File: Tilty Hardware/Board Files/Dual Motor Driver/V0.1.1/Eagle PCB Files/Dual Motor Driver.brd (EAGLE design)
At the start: 50.8 x 50.8 mm, 33 parts, among them J1 AVR_SPI_PRG_6PTH, Q1 16MHz, U1 ATMEGA328P, U2 L298_BRIDGE_DRIVER, U5 VOLTAGE-REGULATOR

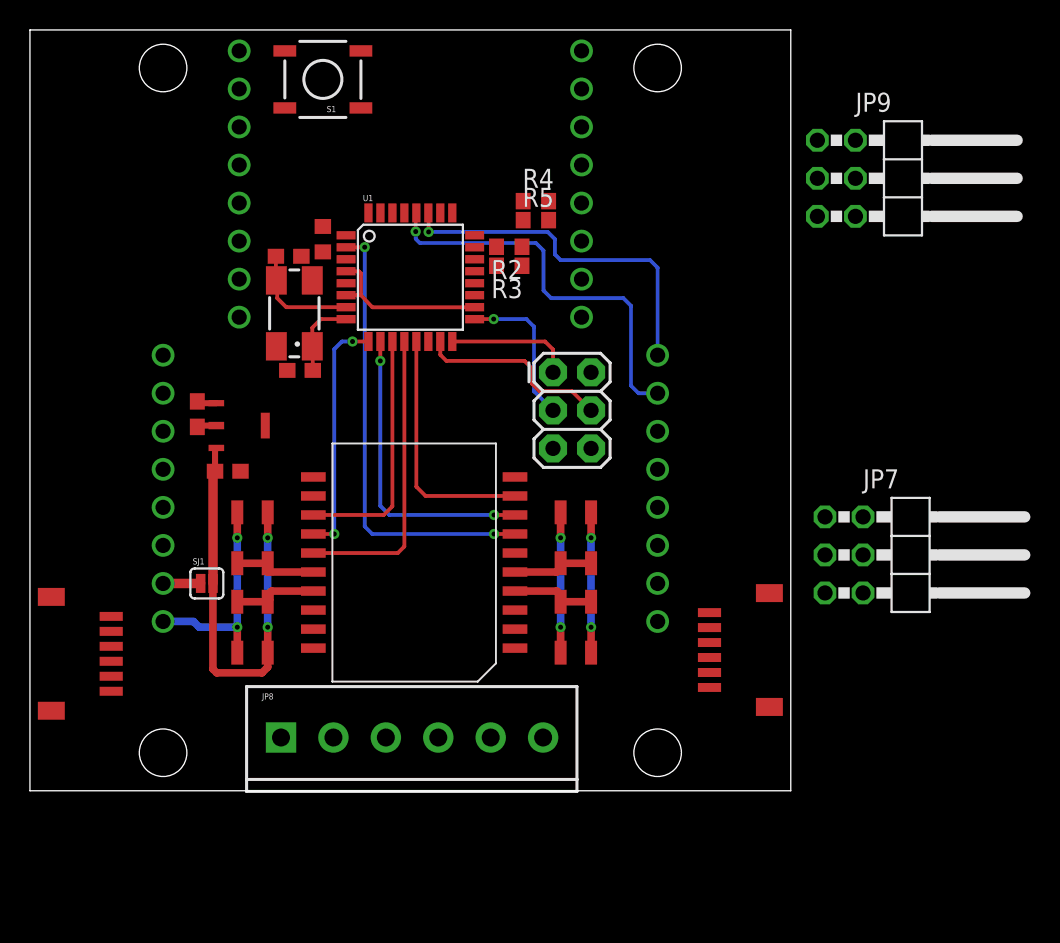
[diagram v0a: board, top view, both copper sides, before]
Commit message: Finished Tilty Duo/Quad 0.2.4, work on motor driver
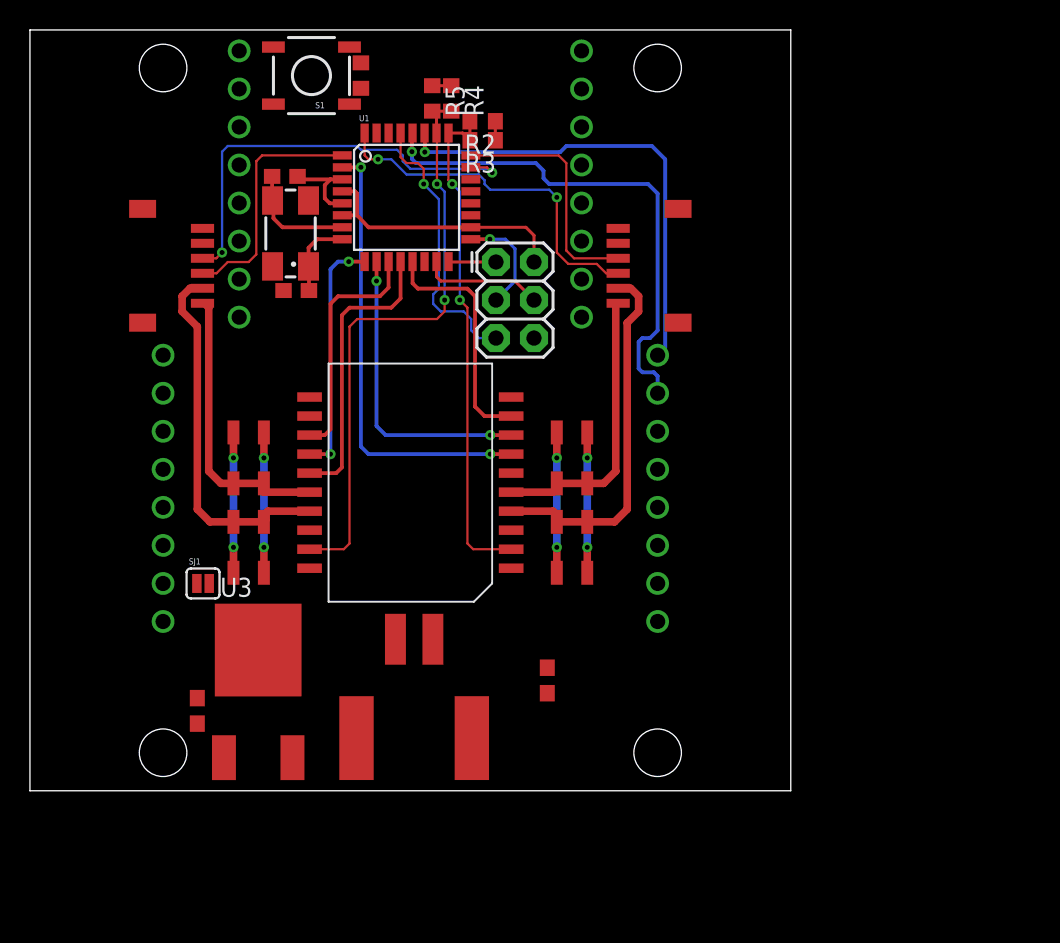
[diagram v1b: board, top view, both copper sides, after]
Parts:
- removed JP8: (no value), SparkFun-Connectors:SCREWTERMINAL-3.5MM-6
- removed JP9: (no value), pinhead:2X03/90
- removed U5: VOLTAGE-REGULATOR, My Parts:SOT89
- added U3: LM2931, on-semiconductor:TO263
- C6: value 0.1uF -> 4.7uF
- C7: value 1uF -> 0.1uF
- JP7: value (none) -> 2-POS_SMD_TERM_BLOCK; device pinhead:2X03/90 -> My Parts:2-POS_SMD_TERMINAL_BLOCK
- moved JP7 35.2 mm to (25.7, 5.84), turned to 0 degrees
- moved C6 29.4 mm to (34.5, 7.37), turned to 90 degrees
- moved JP5 26.6 mm to (9.40, 35.1)
- moved JP6 26.4 mm to (41.4, 35.1)
- moved C7 16.1 mm to (11.2, 5.33), turned to 90 degrees
- moved R1 11.2 mm to (22.1, 47.8)
- moved R5 10.7 mm to (26.9, 46.2), turned to 270 degrees
- moved R4 8.89 mm to (28.1, 46.2), turned to 270 degrees
- moved R2 8.57 mm to (30.2, 44.7)
- moved R3 8.57 mm to (30.2, 43.4)
- moved J1 8.29 mm to (31.1, 35.3)
- moved D2 5.34 mm to (37.2, 22.2)
- moved C2 5.34 mm to (17.8, 33.4)
- moved C8 5.34 mm to (17.0, 41.0)
- moved D3 5.34 mm to (13.6, 22.2)
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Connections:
- net +24V: now also JP7.P$3, U3.P$2; no longer JP8.4, U5.P$3
- net +5V: now also U3.P$3; no longer U5.P$1
- net ENC1B: now also U1.24
- net ENC2A: now also JP5.P$3, U1.23; no longer JP5.P$4, U1.1
- net ENC2B: now also JP5.P$4, U1.1; no longer JP5.P$3
- net GND: now also JP7.P$4, U3.P$1; no longer JP8.3, U5.P$2, U5.P$4
- net M1A: now also JP6.P$2; no longer JP6.P$1, JP8.6
- net M1B: now also JP6.P$1; no longer JP6.P$2, JP8.5
- net M2A: now also JP5.P$6; no longer JP5.P$5, JP8.2
- net M2B: now also JP5.P$5; no longer JP5.P$6, JP8.1
- net SENSE_1: now also U1.25; no longer U1.23
- net SENSE_2: now also U1.26; no longer U1.24
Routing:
- net SENSE_2: track 0.00 -> 39.1 mm, vias 0 -> 2
- net SENSE_1: track 0.00 -> 33.9 mm, vias 0 -> 2
- net ENC2A: track 0.00 -> 28.9 mm, vias 0 -> 2
- net ENC1A: track 0.00 -> 24.0 mm, vias 0 -> 2
- net +24V: track 38.5 -> 18.7 mm
- net M1A: track 5.64 -> 24.8 mm
- net M2B: track 5.64 -> 24.6 mm
- net RESET: track 0.00 -> 18.7 mm, vias 0 -> 1
- net ENC2B: track 0.00 -> 16.2 mm
- net ENC1B: track 0.00 -> 16.1 mm
- net M1B: track 5.52 -> 19.1 mm
- net M2A: track 5.77 -> 19.2 mm
- net SCL: track 26.9 -> 34.5 mm
- net SDA: track 24.0 -> 31.2 mm
- net MISO: track 8.47 -> 3.18 mm
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
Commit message: Nearly finalized dual motor driver add-on
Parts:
- added D10: (no value), SparkFun-LED:LED-0805
- added D9: (no value), diode:DO214AA
- added JP10, JP9: (no value), SparkFun-Connectors:1X02
- added JP8: (no value), SparkFun-Connectors:1X04_LOCK
- added R6: (no value), resistor:R0603
- added SJ2: (no value), SparkFun-Passives:SJ_2S-TRACE
- JP1, JP2, JP3, JP4: value (none) -> 8-PIN_HEADER; device pinhead:1X08_NO_SS -> My Parts:8-PIN_RECEPTACLE_LOCK_NO-SS
- moved C7 18.4 mm to (28.4, 11.7), turned to 270 degrees
- moved U3 12.6 mm to (27.8, 6.35), turned to 180 degrees
- moved C6 8.54 mm to (27.2, 11.7), turned to 270 degrees
- moved JP7 6.48 mm to (19.2, 5.59)
- moved D7 6.22 mm to (29.0, 22.2)
- moved D8 6.22 mm to (29.0, 16.3)
- moved R4 6.22 mm to (21.9, 46.2)
- moved U1 6.22 mm to (18.9, 39.6)
- moved C2 6.22 mm to (11.6, 33.4)
- moved C8 6.22 mm to (10.8, 41.0)
- moved D3 6.22 mm to (7.37, 22.2)
- moved D4 6.22 mm to (7.37, 16.3)
- moved D5 6.22 mm to (9.40, 16.3)
- moved D6 6.22 mm to (9.40, 22.2)
- moved JP1 6.22 mm to (7.75, 40.5)
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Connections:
- new net N$1: D10.1, R6.2
- new net N$3: C7.1, D9.A, SJ2.1, U3.P$2
- new net RX: JP8.3, U1.30
- new net TX: JP8.4, U1.31
- net +24V: now also D9.C, SJ2.2; no longer C7.1, U3.P$2
- net +5V: now also JP4.P$1, JP8.1, R6.1; no longer JP4.1
- net GND: now also D10.2, JP2.P$1, JP3.P$1, JP4.P$2, JP8.2, U2.20; no longer JP2.1, JP3.1, JP4.2
- net M1A: now also JP9.2
- net M1B: now also JP9.1
- net M2A: now also JP10.2
- net M2B: now also JP10.1
- net N$5: now also JP2.P$2; no longer JP2.2
- net SCL: now also JP3.P$7; no longer JP3.7
- net SDA: now also JP3.P$8; no longer JP3.8
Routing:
- net GND: track 27.1 -> 276.5 mm, vias 4 -> 20
- net +5V: track 17.7 -> 148.8 mm, vias 0 -> 6
- net +24V: track 18.7 -> 63.7 mm
- net M1B: track 19.1 -> 40.2 mm, vias 0 -> 1
- net M2A: track 19.2 -> 34.4 mm, vias 0 -> 1
- net M1A: track 24.8 -> 37.1 mm
- net M2B: track 24.6 -> 34.4 mm
- net RESET: track 18.7 -> 28.3 mm
- net N$5: track 0.00 -> 8.34 mm
- net N$3: track 0.00 -> 7.67 mm
- net RX: track 0.00 -> 7.36 mm, vias 0 -> 1
- net TX: track 0.00 -> 6.03 mm, vias 0 -> 1
- net N$1: track 0.00 -> 1.86 mm
- net SDA: track 31.2 -> 29.4 mm
- net SCL: track 34.5 -> 32.9 mm
- added copper zone on layer 1, net GND
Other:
- board size 50.8 x 50.8 mm -> 38.4 x 50.8 mm
- board text added: "+"
- board text added: "-"
- board text added: "5v"
- board text added: "Driver Add-on"
- board text added: "Dual Motor"
- board text added: "GND"
- board text added: "ICSP"
- board text added: "IMU"
- board text added: "M1A"
- board text added: "M1B"
- board text added: "M2A"
- board text added: "M2B"
- board text added: "PWR"
- board text added: "Reset"
- board text added: "Rx"
- board text added: "SJ1"
- board text added: "Tx"

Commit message: New RC Receiver add-on testing code and minor motor driver updates
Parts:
- J1: value AVR_SPI_PRG_6PTH -> AVR_SPI_PRG_62X3_LOCK; device SparkFun-Connectors:2X3 -> SparkFun-Connectors:2X3_LOCK
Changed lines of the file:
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@@
 <attribute name="PART#" value="SM06B-SRSS-TB(LF)(SN)" x="35.179" y="35.052" size="1.778" layer="27" rot="R90" display="off"/>
 </element>
-<element name="J1" library="SparkFun-Connectors" package="2X3" value="AVR_SPI_PRG_6PTH" x="24.892" y="35.306" smashed="yes" rot="R270"/>
+<element name="J1" library="SparkFun-Connectors" package="2X3_LOCK" value="AVR_SPI_PRG_62X3_LOCK" x="24.892" y="35.306" smashed="yes" rot="R270"/>
 <element name="R1" library="resistor" package="R0603" value="10K" x="19.3675" y="46.228" smashed="yes" rot="R90"/>
 <element name="C6" library="resistor" package="C0603" value="4.7uF" x="27.178" y="11.684" smashed="yes" rot="R270"/>
@@
 <wire x1="24.4856" y1="36.83" x2="23.2216" y2="36.83" width="0.254" layer="1"/>
 <wire x1="23.2216" y1="36.83" x2="23.2156" y2="36.824" width="0.254" layer="1"/>
-<wire x1="24.892" y1="32.766" x2="26.162" y2="34.036" width="0.2032" layer="16"/>
+<wire x1="24.638" y1="32.766" x2="26.162" y2="34.036" width="0.2032" layer="16"/>
 <wire x1="26.162" y1="34.036" x2="26.162" y2="36.195" width="0.2032" layer="16"/>
 <wire x1="26.162" y1="36.195" x2="25.527" y2="36.83" width="0.2032" layer="16"/>
@@
 <wire x1="20.923" y1="34.322" x2="21.209" y2="34.036" width="0.2032" layer="1"/>
 <wire x1="21.209" y1="34.036" x2="26.162" y2="34.036" width="0.2032" layer="1"/>
-<wire x1="26.162" y1="34.036" x2="27.432" y2="32.766" width="0.2032" layer="1"/>
+<wire x1="26.162" y1="34.036" x2="27.178" y2="32.766" width="0.2032" layer="1"/>
 </signal>
 <signal name="MISO">
@@
 <contactref element="U1" pad="13"/>
 <wire x1="25.908" y1="25.019" x2="24.13" y2="25.019" width="0.254" layer="1"/>
-<wire x1="24.13" y1="25.019" x2="23.495" y2="25.654" width="0.254" layer="1"/>
-<wire x1="23.495" y1="25.654" x2="23.495" y2="33.02" width="0.254" layer="1"/>
-<wire x1="23.495" y1="33.02" x2="22.987" y2="33.528" width="0.254" layer="1"/>
+<wire x1="24.13" y1="25.019" x2="23.4315" y2="25.7175" width="0.254" layer="1"/>
+<wire x1="23.4315" y1="25.7175" x2="23.368" y2="33.147" width="0.254" layer="1"/>
+<wire x1="23.368" y1="33.147" x2="22.987" y2="33.528" width="0.254" layer="1"/>
 <wire x1="19.323" y1="35.3314" x2="19.323" y2="33.89" width="0.254" layer="1"/>
 <wire x1="19.323" y1="33.89" x2="19.685" y2="33.528" width="0.254" layer="1"/>

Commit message: Tilty Omni work!
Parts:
- moved D10 0.97 mm to (11.2, 2.92), turned to 180 degrees
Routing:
- net GND: track 276.5 -> 274.4 mm
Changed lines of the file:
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@@
 <text x="18.415" y="48.1965" size="1.524" layer="26" ratio="10" rot="MR270">Tx</text>
 <text x="17.907" y="29.464" size="1.651" layer="25" ratio="12">ICSP</text>
-<text x="6.477" y="1.778" size="1.651" layer="25" ratio="12">PWR</text>
+<text x="6.985" y="4.318" size="1.651" layer="25" ratio="12">PWR</text>
 <rectangle x1="23.13594375" y1="18.232378125" x2="23.27818125" y2="18.252696875" layer="26" rot="R213"/>
 <rectangle x1="23.10455" y1="18.249421875" x2="23.28743125" y2="18.269740625" layer="26" rot="R213"/>
@@
 <rectangle x1="14.3174" y1="21.635384375" x2="14.5206" y2="21.655703125" layer="26" rot="R213"/>
 <rectangle x1="14.3096125" y1="21.641359375" x2="14.472175" y2="21.661678125" layer="26" rot="R213"/>
-<rectangle x1="46.195865625" y1="25.53190625" x2="46.317784375" y2="25.552225" layer="26" rot="R213"/>
-<rectangle x1="46.24411875" y1="25.554478125" x2="46.2644375" y2="25.574796875" layer="26" rot="R213"/>
 <text x="20.004971875" y="17.009321875" size="1.905" layer="26" font="vector" ratio="17" rot="MR2">IMU</text>
 <text x="24.765" y="15.494" size="1.27" layer="26" ratio="12" rot="MR0">Dual Motor</text>
@@
 <attribute name="VALUE" x="4.572" y="39.878" size="1.27" layer="27" rot="R90"/>
 </element>
-<element name="D10" library="SparkFun-LED" package="LED-0805" value="" x="12.065" y="2.54" smashed="yes" rot="R270">
-<attribute name="VALUE" x="9.144" y="3.302" size="1.27" layer="27" rot="R270"/>
+<element name="D10" library="SparkFun-LED" package="LED-0805" value="" x="11.176" y="2.921" smashed="yes" rot="R180">
+<attribute name="VALUE" x="11.938" y="5.842" size="1.27" layer="27" rot="R180"/>
 </element>
 <element name="R6" library="resistor" package="R0603" value="" x="12.065" y="6.096" smashed="yes" rot="R270">
@@
 <wire x1="23.495" y1="46.863" x2="30.734" y2="46.863" width="0.3175" layer="16"/>
 <contactref element="D10" pad="2"/>
-<wire x1="12.065" y1="1.69" x2="11.137" y2="1.69" width="0.254" layer="1"/>
-<wire x1="11.137" y1="1.69" x2="10.795" y2="2.032" width="0.254" layer="1"/>
-<wire x1="10.795" y1="2.032" x2="10.795" y2="9.144" width="0.254" layer="1"/>
 <wire x1="10.795" y1="9.144" x2="10.541" y2="9.398" width="0.254" layer="1"/>
 <wire x1="10.541" y1="9.398" x2="6.477" y2="9.398" width="0.254" layer="1"/>
@@
 <vertex x="13.462" y="12.446"/>
 </polygon>
+<wire x1="10.795" y1="9.144" x2="10.795" y2="3.39" width="0.254" layer="1"/>
+<wire x1="10.795" y1="3.39" x2="10.326" y2="2.921" width="0.254" layer="1"/>
 </signal>
 <signal name="M1A">
@@
 <contactref element="D10" pad="1"/>
 <contactref element="R6" pad="2"/>
-<wire x1="12.065" y1="5.246" x2="12.065" y2="3.39" width="0.254" layer="1"/>
+<wire x1="12.065" y1="5.246" x2="12.026" y2="2.921" width="0.254" layer="1"/>
 </signal>
 </signals>

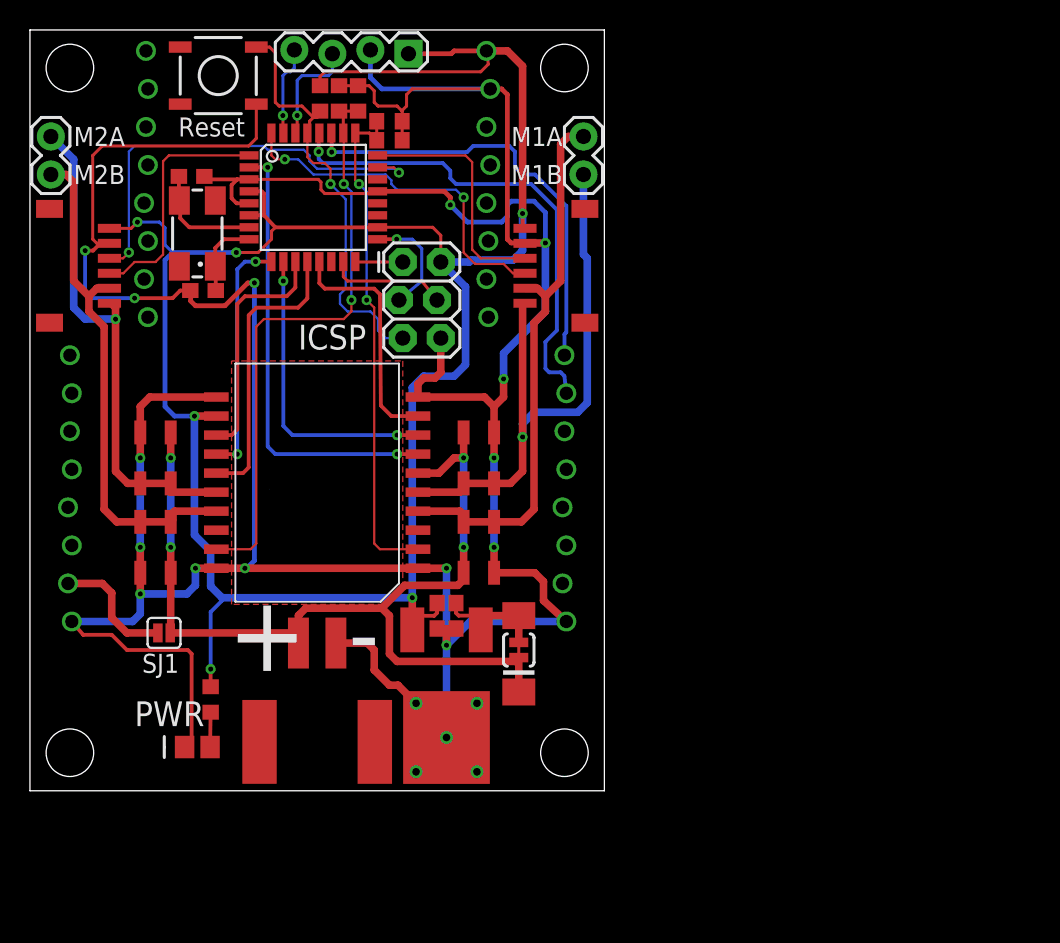
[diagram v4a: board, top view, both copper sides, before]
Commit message: Motor driver: added test code, updated things.todo, some hardware updates
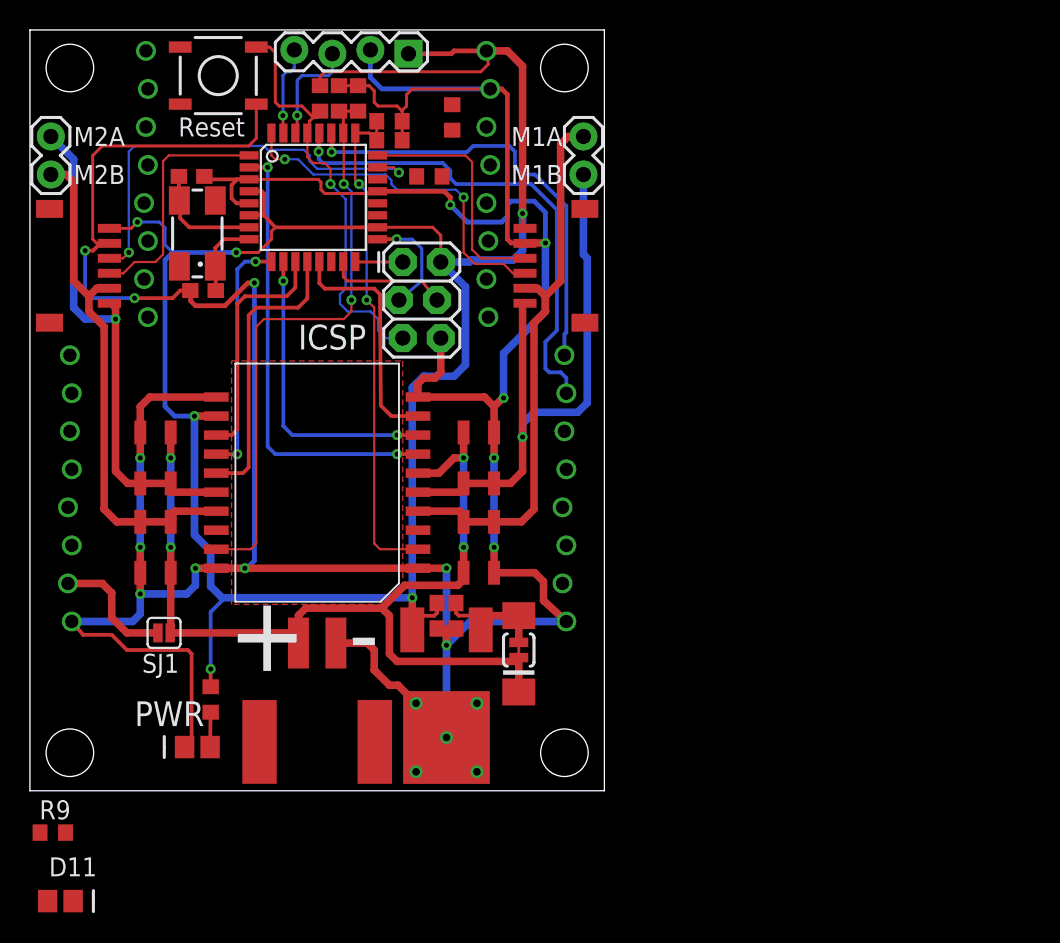
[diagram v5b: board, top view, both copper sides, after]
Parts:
- added D11: (no value), SparkFun-LED:LED-0805
- added R7, R8, R9: (no value), resistor:R0603
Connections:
- net +5V: now also R7.2, R8.2
- net SCL: now also R8.1
- net SDA: now also R7.1
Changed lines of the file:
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@@
 <attribute name="VALUE" x="10.033" y="6.985" size="1.27" layer="27" rot="R270"/>
 </element>
+<element name="R7" library="resistor" package="R0603" value="" x="28.194" y="44.958" smashed="yes" rot="R90">
+<attribute name="VALUE" x="30.226" y="44.069" size="1.27" layer="27" rot="R90"/>
+</element>
+<element name="R8" library="resistor" package="R0603" value="" x="26.67" y="41.021" smashed="yes" rot="R180">
+<attribute name="VALUE" x="27.559" y="43.053" size="1.27" layer="27" rot="R180"/>
+</element>
+<element name="R9" library="resistor" package="R0603" value="" x="1.524" y="-2.794"/>
+<element name="D11" library="SparkFun-LED" package="LED-0805" value="" x="2.032" y="-7.366"/>
 </elements>
 <signals>
@@
 <wire x1="7.366" y1="25.654" x2="8.001" y2="26.289" width="0.508" layer="1"/>
 <wire x1="8.001" y1="26.289" x2="12.446" y2="26.289" width="0.508" layer="1"/>
-<via x="31.623" y="27.4955" extent="1-16" drill="0.3302"/>
+<via x="31.623" y="26.2255" extent="1-16" drill="0.3302"/>
 <via x="34.417" y="36.576" extent="1-16" drill="0.3302"/>
-<wire x1="31.623" y1="27.4955" x2="31.623" y2="26.289" width="0.508" layer="1"/>
+<wire x1="31.623" y1="26.2255" x2="31.623" y2="26.289" width="0.508" layer="1"/>
 <wire x1="31.623" y1="26.289" x2="30.988" y2="25.654" width="0.508" layer="1"/>
 <wire x1="34.417" y1="36.576" x2="34.417" y2="32.004" width="0.508" layer="16"/>
 <wire x1="34.417" y1="32.004" x2="31.623" y2="29.21" width="0.508" layer="16"/>
-<wire x1="31.623" y1="29.21" x2="31.623" y2="27.4955" width="0.508" layer="16"/>
+<wire x1="31.623" y1="29.21" x2="31.623" y2="26.2255" width="0.508" layer="16"/>
 <wire x1="34.417" y1="36.576" x2="33.078" y2="36.576" width="0.508" layer="1"/>
 <wire x1="33.078" y1="36.576" x2="33.054" y2="36.552" width="0.508" layer="1"/>
@@
 <wire x1="12.065" y1="11.938" x2="12.065" y2="8.128" width="0.254" layer="16"/>
 <wire x1="12.065" y1="8.128" x2="12.065" y2="6.946" width="0.254" layer="1"/>
+<contactref element="R7" pad="2"/>
+<contactref element="R8" pad="2"/>
+<wire x1="25.273" y1="49.2125" x2="28.194" y2="45.808" width="0" layer="19" extent="1-1"/>
+<wire x1="25.82" y1="41.021" x2="29.083" y2="28.448" width="0" layer="19" extent="1-16"/>
 </signal>
 <signal name="RESET">
@@
 <wire x1="35.814" y1="30.607" x2="35.687" y2="30.48" width="0.254" layer="16"/>
 <wire x1="35.687" y1="30.48" x2="35.687" y2="29.083" width="0.254" layer="16"/>
+<contactref element="R7" pad="1"/>
+<wire x1="29.1846" y1="42.6466" x2="28.194" y2="44.108" width="0" layer="19" extent="1-16"/>
 </signal>
 <signal name="SCL">
@@
 <wire x1="34.417" y1="28.194" x2="34.671" y2="27.94" width="0.254" layer="16"/>
 <wire x1="34.671" y1="27.94" x2="35.433" y2="27.94" width="0.254" layer="16"/>
-<wire x1="35.433" y1="27.94" x2="35.687" y2="27.686" width="0.254" layer="16"/>
-<wire x1="35.687" y1="27.686" x2="35.814" y2="26.543" width="0.254" layer="16"/>
+<wire x1="35.433" y1="27.94" x2="35.814" y2="27.559" width="0.254" layer="16"/>
+<wire x1="35.814" y1="27.559" x2="35.814" y2="26.543" width="0.254" layer="16"/>
 <wire x1="34.417" y1="29.972" x2="35.179" y2="30.734" width="0.254" layer="16"/>
 <wire x1="35.179" y1="30.734" x2="35.179" y2="38.7985" width="0.254" layer="16"/>
 <wire x1="35.179" y1="38.7985" x2="33.4645" y2="40.513" width="0.254" layer="16"/>
 <wire x1="33.4645" y1="40.513" x2="28.448" y2="40.513" width="0.254" layer="16"/>
+<contactref element="R8" pad="1"/>
+<wire x1="27.52" y1="41.021" x2="34.417" y2="28.194" width="0" layer="19" extent="1-16"/>
 </signal>
 <signal name="ENC1B">
